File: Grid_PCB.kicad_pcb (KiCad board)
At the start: 2 copper layers, 223.2 x 22 mm, 41 parts, among them J1 Conn_01x04_Female, J10 LED_Conn, J11 ESP_Conn, J2 Conn_01x04_Female, J3 Conn_01x04_Female, J4 Conn_01x04_Female, J5 Conn_01x04_Female, J6 Conn_01x04_Female, J7 Conn_01x04_Female, J8 Conn_01x04_Female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

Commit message: minor fix to mux strobe (enable) pin
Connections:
- U1 pad 7: Net-(U1-Pad7) -> GND

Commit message: updated conns and mounting holes
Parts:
- J10, J11: footprint Connector_JST:JST_EH_B2B-EH-A_1x02_P2.50mm_Vertical -> conn:TE_640456-2
- J9: footprint Connector_JST:JST_EH_B5B-EH-A_1x05_P2.50mm_Vertical -> conn:TE_640456-5
- moved H2 50.6 mm to (142.5, 89.0)
- moved H3 28.1 mm to (194.4, 100.4)
- moved H4 12.6 mm to (244.7, 89.1)
- moved J10 2.14 mm to (261.9, 85.9), turned to 90 degrees
- moved J9 1.21 mm to (46.9, 96.4), turned to 270 degrees
- moved H1 0.93 mm to (69.9, 98.9)
- moved J11 0.60 mm to (47.0, 103.0), turned to 270 degrees
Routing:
- net /ESPselA: track 6.51 -> 20.0 mm
- net /ESPselC: track 18.6 -> 24.7 mm
- net /LED_In: track 225.9 -> 231.6 mm
- net /ESPselB: track 13.3 -> 9.72 mm
- net /BTN3: track 97.3 -> 98.6 mm
- net /MUX_OUT: track 18.6 -> 19.9 mm
- net /LED_Out: track 9.69 -> 10.5 mm
- net GND: vias 13 -> 14

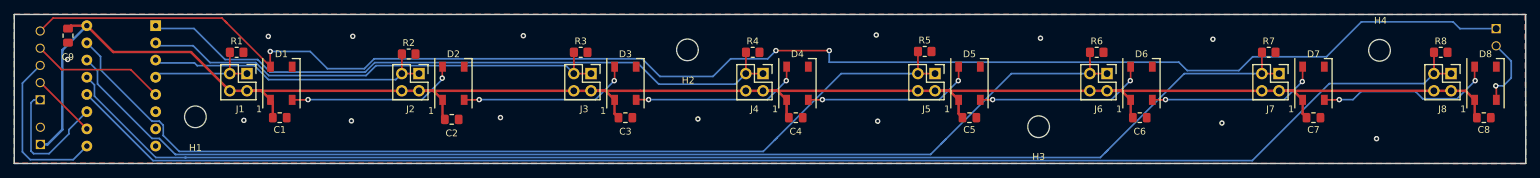
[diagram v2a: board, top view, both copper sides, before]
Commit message: updated jst footprint/library and updated routing on sel signals
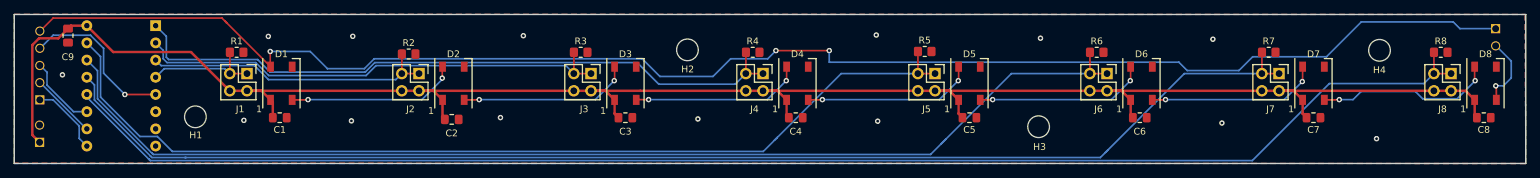
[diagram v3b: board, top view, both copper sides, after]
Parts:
- J10: footprint conn:TE_640456-2 -> JST_Conn:TE_640456-2
- J11: value ESP_Conn -> Power_Conn; footprint conn:TE_640456-2 -> JST_Conn:TE_640456-2
- J9: footprint conn:TE_640456-5 -> JST_Conn:TE_640456-5
- moved J11 0.34 mm to (46.8, 102.7)
- moved J10 0.07 mm to (261.9, 85.9)
- moved J9 0.05 mm to (46.9, 96.4)
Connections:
- J9 pad 1: /ESPselA -> /ESPselC
- J9 pad 3: /ESPselC -> /ESPselA
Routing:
- net /ESPselC: track 24.7 -> 10.9 mm
- net /ESPselA: track 20.0 -> 10.9 mm
- net /MUX_OUT: track 19.9 -> 23.6 mm, vias 0 -> 1
- net /BTN4: track 142.5 -> 144.0 mm
- net /BTN5: track 166.7 -> 168.1 mm
- net /BTN3: track 98.6 -> 100.0 mm

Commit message: first attempt at waves
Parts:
- added G***: LOGO, grid:Wave, F.Cu at (68.3, 92.9)
- added G***: LOGO, grid:Wave, F.Cu at (248.0, 93.0)
- added G***: LOGO, grid:Wave, F.Cu at (221.7, 93.4)
- added G***: LOGO, grid:Wave, F.Cu at (196.3, 93.2)
- added G***: LOGO, grid:Wave, F.Cu at (170.9, 93.1)
- added G***: LOGO, grid:Wave, F.Cu at (145.3, 93.1)
- added G***: LOGO, grid:Wave, F.Cu at (119.7, 93.2)
- added G***: LOGO, grid:Wave, F.Cu at (94.1, 93.2)

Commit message: wave pattern attempt
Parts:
- removed the G*** at (68.3, 92.9)
- removed the G*** at (248.0, 93.0)
- removed the G*** at (221.7, 93.4)
- removed the G*** at (196.3, 93.2)
- removed the G*** at (170.9, 93.1)
- removed the G*** at (145.3, 93.1)
- removed the G*** at (119.7, 93.2)
- removed the G*** at (94.1, 93.2)
- added G***: LOGO, grid:wave_pattern, F.Cu at (153.9, 95.1)

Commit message: wave 2
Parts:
- removed the G*** at (153.9, 95.1)
- added G***: LOGO, grid:wave_pattern_2_light, F.Cu at (154.1, 95.1)
- added G***: LOGO, grid:wave_pattern_2, F.Cu at (154.9, 94.6)

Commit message: wave 2 light
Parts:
- removed the G*** at (154.9, 94.6)
- moved G*** 0.72 mm to (154.8, 94.9)

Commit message: wave 3
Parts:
- removed the G*** at (154.8, 94.9)
- added G***: LOGO, grid:wave_pattern_3, F.Cu at (154.3, 94.9)
